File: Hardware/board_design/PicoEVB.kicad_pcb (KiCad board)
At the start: 4 copper layers, 22.5 x 30 mm, 107 parts, among them J1 RX-, J10 1P2, J11 1P0, J12 GND, J2 RX+, J3 CLKIN-, J4 CLKIN+, J5 TX+, J6 TX-, J7 3P3, J8 1P8, J9 1P0, P1 CONN_01X06, U1 XC7AxxT-xCSG325, U2 S25Q, U3 TPS82085SIL, U4 MAX1589AETT100T, U5 MIC47050-1.2YML, U6 TPS82085SIL, U7 FT230XQ

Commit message: configure project libararies
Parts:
- added REF**: VFBGA54, AS4C32M16MSA-6BIN:AS4C32M16MSA-6BIN, F.Cu at (84.9, 80.9)

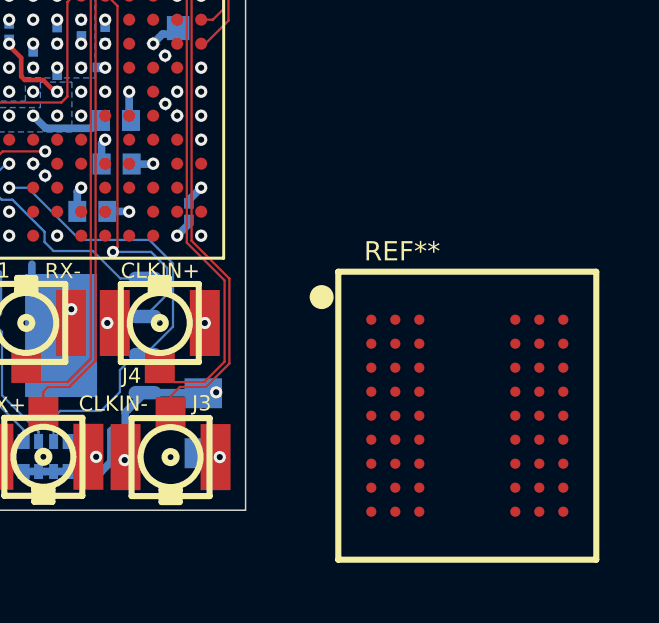
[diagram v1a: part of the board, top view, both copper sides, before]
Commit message: Added LPSDRAM
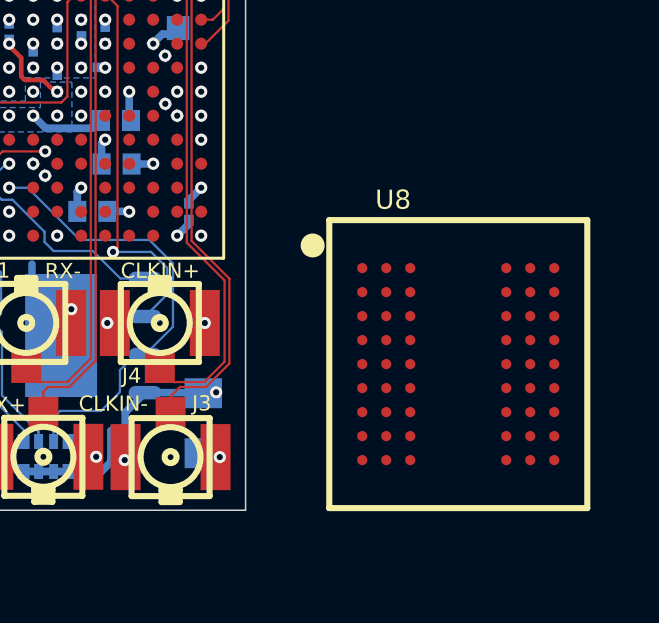
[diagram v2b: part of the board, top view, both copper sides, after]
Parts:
- removed REF**: VFBGA54, AS4C32M16MSA-6BIN:AS4C32M16MSA-6BIN
- added U8: VFBGA54, AS4C32M16MSA-6BIN:AS4C32M16MSA-6BIN, F.Cu at (84.6, 79.2)
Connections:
- PCB1 pad 55: (no net) -> Net-(PCB1-Pad55)
- RN1 pad 5: (no net) -> Net-(RN1-Pad5)
- RN3 pad 8: (no net) -> Net-(RN3-Pad8)
- U1 pad A15: (no net) -> Net-(U1-PadA15)
- U1 pad A17: (no net) -> Net-(U1-PadA17)
- U1 pad B10: (no net) -> Net-(U1-PadB10)
- U1 pad B11: (no net) -> Net-(U1-PadB11)
- U1 pad B14: (no net) -> Net-(U1-PadB14)
- U1 pad B15: (no net) -> Net-(U1-PadB15)
- U1 pad B16: (no net) -> Net-(U1-PadB16)
- U1 pad B17: (no net) -> Net-(U1-PadB17)
- U1 pad B9: (no net) -> Net-(U1-PadB9)
- U1 pad C11: (no net) -> Net-(U1-PadC11)
- U1 pad C12: (no net) -> Net-(U1-PadC12)
- U1 pad C13: (no net) -> Net-(U1-PadC13)
- U1 pad C14: (no net) -> Net-(U1-PadC14)
- U1 pad C16: (no net) -> Net-(U1-PadC16)
- U1 pad C17: (no net) -> Net-(U1-PadC17)
- U1 pad C18: (no net) -> Net-(U1-PadC18)
- U1 pad C8: (no net) -> Net-(U1-PadC8)
- U1 pad C9: (no net) -> Net-(U1-PadC9)
- U1 pad D10: (no net) -> Net-(U1-PadD10)
- U1 pad D11: (no net) -> Net-(U1-PadD11)
- U1 pad D13: (no net) -> Net-(U1-PadD13)
- U1 pad D14: (no net) -> Net-(U1-PadD14)
- U1 pad D15: (no net) -> Net-(U1-PadD15)
- U1 pad D16: (no net) -> Net-(U1-PadD16)
- U1 pad D18: (no net) -> Net-(U1-PadD18)
- U1 pad D8: (no net) -> Net-(U1-PadD8)
- U1 pad D9: (no net) -> Net-(U1-PadD9)
- U1 pad E13: (no net) -> Net-(U1-PadE13)
- U1 pad E15: (no net) -> Net-(U1-PadE15)
- U1 pad E16: (no net) -> Net-(U1-PadE16)
- U1 pad E17: (no net) -> Net-(U1-PadE17)
- U1 pad E18: (no net) -> Net-(U1-PadE18)
- U1 pad F1: (no net) -> Net-(U1-PadF1)
- U1 pad F14: (no net) -> Net-(U1-PadF14)
- U1 pad F15: (no net) -> Net-(U1-PadF15)
- U1 pad F17: (no net) -> Net-(U1-PadF17)
- U1 pad F18: (no net) -> Net-(U1-PadF18)
- U1 pad F2: (no net) -> Net-(U1-PadF2)
- U1 pad G14: (no net) -> Net-(U1-PadG14)
- U1 pad G15: (no net) -> Net-(U1-PadG15)
- U1 pad G16: (no net) -> Net-(U1-PadG16)
- U1 pad G17: (no net) -> Net-(U1-PadG17)
- U1 pad H14: (no net) -> Net-(U1-PadH14)
- U1 pad H16: (no net) -> Net-(U1-PadH16)
- U1 pad H17: (no net) -> Net-(U1-PadH17)
- U1 pad H18: (no net) -> Net-(U1-PadH18)
- U1 pad J14: (no net) -> Net-(U1-PadJ14)
- U1 pad J4: (no net) -> Net-(U1-PadJ4)
- U1 pad J5: (no net) -> Net-(U1-PadJ5)
- U1 pad J6: (no net) -> Net-(U1-PadJ6)
- U1 pad K15: (no net) -> Net-(U1-PadK15)
- U1 pad K17: (no net) -> Net-(U1-PadK17)
- U1 pad K18: (no net) -> Net-(U1-PadK18)
- U1 pad K3: (no net) -> Net-(U1-PadK3)
- U1 pad K5: (no net) -> Net-(U1-PadK5)
- U1 pad K6: (no net) -> Net-(U1-PadK6)
- U1 pad L14: (no net) -> Net-(U1-PadL14)
- U1 pad L18: (no net) -> Net-(U1-PadL18)
- U1 pad L2: (no net) -> Net-(U1-PadL2)
- U1 pad L3: (no net) -> Net-(U1-PadL3)
- U1 pad L4: (no net) -> Net-(U1-PadL4)
- U1 pad L5: (no net) -> Net-(U1-PadL5)
- U1 pad M1: (no net) -> Net-(U1-PadM1)
- U1 pad M14: (no net) -> Net-(U1-PadM14)
- U1 pad M15: (no net) -> Net-(U1-PadM15)
- U1 pad M16: (no net) -> Net-(U1-PadM16)
- U1 pad M17: (no net) -> Net-(U1-PadM17)
- U1 pad M2: (no net) -> Net-(U1-PadM2)
- U1 pad M4: (no net) -> Net-(U1-PadM4)
- U1 pad M5: (no net) -> Net-(U1-PadM5)
- U1 pad M6: (no net) -> Net-(U1-PadM6)
- U1 pad N1: (no net) -> Net-(U1-PadN1)
- U1 pad N14: (no net) -> Net-(U1-PadN14)
- U1 pad N16: (no net) -> Net-(U1-PadN16)
- U1 pad N17: (no net) -> Net-(U1-PadN17)
- U1 pad N18: (no net) -> Net-(U1-PadN18)
- U1 pad N2: (no net) -> Net-(U1-PadN2)
- U1 pad N3: (no net) -> Net-(U1-PadN3)
- U1 pad N4: (no net) -> Net-(U1-PadN4)
- U1 pad N6: (no net) -> Net-(U1-PadN6)
- U1 pad P1: (no net) -> Net-(U1-PadP1)
- U1 pad P14: (no net) -> Net-(U1-PadP14)
- U1 pad P15: (no net) -> Net-(U1-PadP15)
- U1 pad P16: (no net) -> Net-(U1-PadP16)
- U1 pad P18: (no net) -> Net-(U1-PadP18)
- U1 pad P3: (no net) -> Net-(U1-PadP3)
- U1 pad P4: (no net) -> Net-(U1-PadP4)
- U1 pad P5: (no net) -> Net-(U1-PadP5)
- U1 pad P6: (no net) -> Net-(U1-PadP6)
- U1 pad R1: (no net) -> Net-(U1-PadR1)
- U1 pad R13: (no net) -> Net-(U1-PadR13)
- U1 pad R15: (no net) -> Net-(U1-PadR15)
- U1 pad R16: (no net) -> Net-(U1-PadR16)
- U1 pad R17: (no net) -> Net-(U1-PadR17)
- U1 pad R18: (no net) -> Net-(U1-PadR18)
- U1 pad R2: (no net) -> Net-(U1-PadR2)
- U1 pad R3: (no net) -> Net-(U1-PadR3)
- U1 pad R5: (no net) -> Net-(U1-PadR5)
- U1 pad R6: (no net) -> Net-(U1-PadR6)
- U1 pad R7: (no net) -> Net-(U1-PadR7)
- U1 pad T12: (no net) -> Net-(U1-PadT12)
- U1 pad T13: (no net) -> Net-(U1-PadT13)
- U1 pad T14: (no net) -> Net-(U1-PadT14)
- U1 pad T15: (no net) -> Net-(U1-PadT15)
- U1 pad T17: (no net) -> Net-(U1-PadT17)
- U1 pad T18: (no net) -> Net-(U1-PadT18)
- U1 pad T2: (no net) -> Net-(U1-PadT2)
- U1 pad T3: (no net) -> Net-(U1-PadT3)
- U1 pad T4: (no net) -> Net-(U1-PadT4)
- U1 pad T5: (no net) -> Net-(U1-PadT5)
- U1 pad T7: (no net) -> Net-(U1-PadT7)
- U1 pad U1: (no net) -> Net-(U1-PadU1)
- U1 pad U10: (no net) -> Net-(U1-PadU10)
- U1 pad U11: (no net) -> Net-(U1-PadU11)
- U1 pad U12: (no net) -> Net-(U1-PadU12)
- U1 pad U14: (no net) -> Net-(U1-PadU14)
- U1 pad U15: (no net) -> Net-(U1-PadU15)
- U1 pad U16: (no net) -> Net-(U1-PadU16)
- U1 pad U17: (no net) -> Net-(U1-PadU17)
- U1 pad U2: (no net) -> Net-(U1-PadU2)
- U1 pad U4: (no net) -> Net-(U1-PadU4)
- U1 pad U5: (no net) -> Net-(U1-PadU5)
- U1 pad U6: (no net) -> Net-(U1-PadU6)
- U1 pad U7: (no net) -> Net-(U1-PadU7)
- U1 pad U9: (no net) -> Net-(U1-PadU9)
- U1 pad V11: (no net) -> Net-(U1-PadV11)
- U1 pad V16: (no net) -> Net-(U1-PadV16)
- U1 pad V17: (no net) -> Net-(U1-PadV17)
- U1 pad V4: (no net) -> Net-(U1-PadV4)
- U1 pad V6: (no net) -> Net-(U1-PadV6)
- U1 pad V7: (no net) -> Net-(U1-PadV7)
- U1 pad V8: (no net) -> Net-(U1-PadV8)
- U1 pad V9: (no net) -> Net-(U1-PadV9)
- U4 pad 2: (no net) -> Net-(U4-Pad2)
- U4 pad 3: (no net) -> Net-(U4-Pad3)
- U5 pad 5: (no net) -> Net-(U5-Pad5)
- U7 pad 11: (no net) -> Net-(U7-Pad11)
- U7 pad 12: (no net) -> Net-(U7-Pad12)
- U7 pad 14: (no net) -> Net-(U7-Pad14)
- U7 pad 5: (no net) -> Net-(U7-Pad5)

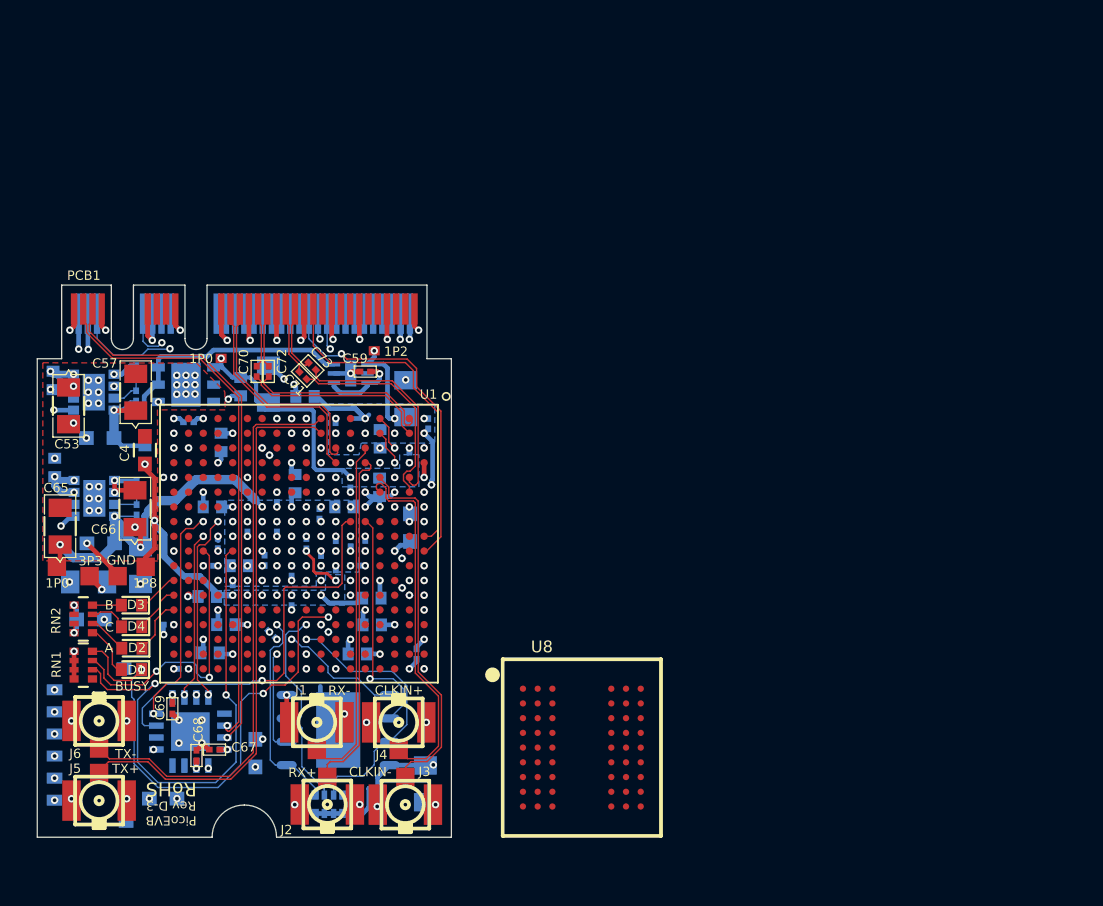
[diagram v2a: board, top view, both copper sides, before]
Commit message: populate LPSDRAM IC
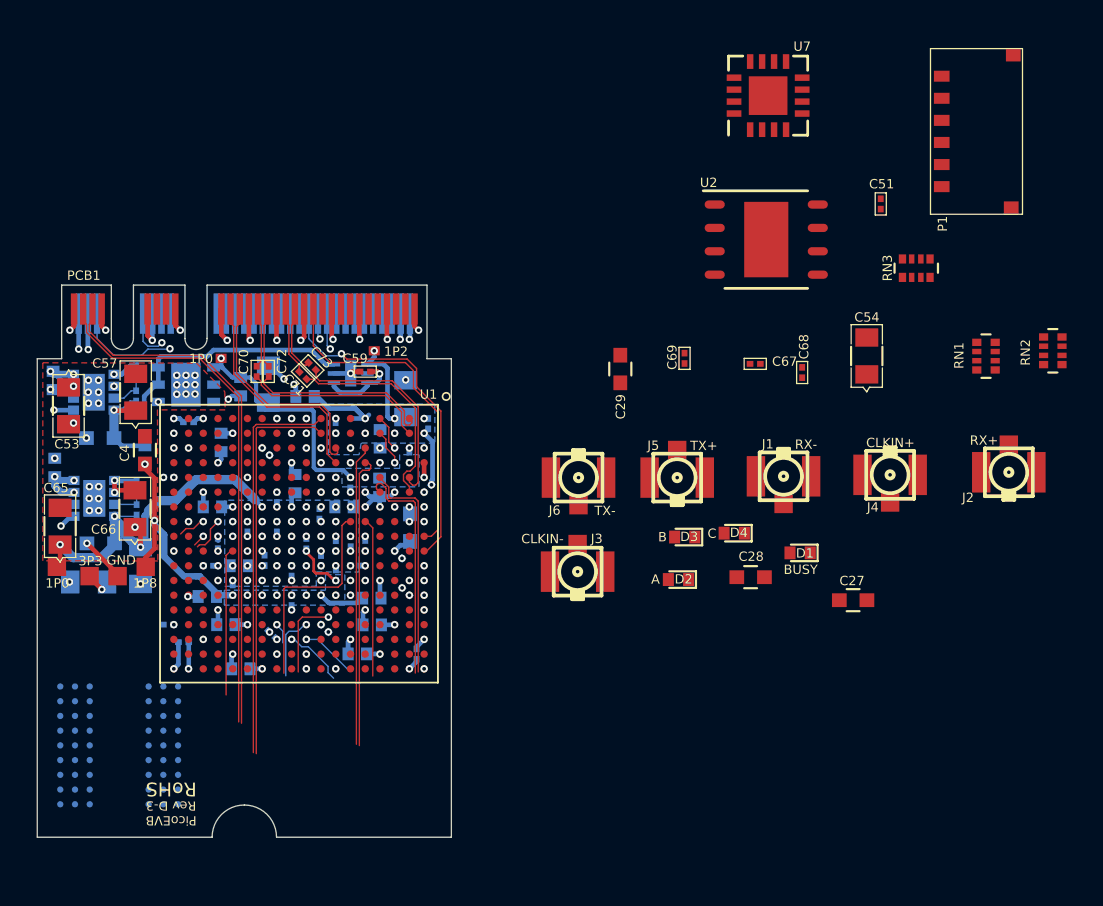
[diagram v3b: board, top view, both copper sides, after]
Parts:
- C27, C28, C29, C51, C54, P1, RN3, U2, U7: moved to F.Cu
- U8: moved to B.Cu
- moved P1 58.6 mm to (106.1, 45.7), turned to 90 degrees
- moved RN2 54.7 mm to (110.2, 57.6)
- moved RN1 51.8 mm to (106.6, 57.9)
- moved U7 46.7 mm to (94.7, 43.8), turned to 90 degrees
- moved RN3 43.2 mm to (102.8, 53.1), turned to 270 degrees
- moved C51 42.1 mm to (100.8, 49.7), turned to 90 degrees
- moved C27 41.5 mm to (99.3, 71.2)
- moved J2 41.2 mm to (107.8, 64.2)
- moved C68 38.9 mm to (96.6, 58.8)
- moved D1 36.9 mm to (96.5, 68.6)
- moved C67 36.1 mm to (94.0, 58.4)
- moved J5 36.0 mm to (89.8, 64.5)
- moved U2 35.4 mm to (94.6, 51.6)
- moved C28 34.1 mm to (93.8, 69.9)
- moved C69 33.7 mm to (90.2, 58.0)
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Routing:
- net Net-(D1-Pad1): track 31.0 -> 7.44 mm, vias 4 -> 2
- net Net-(RN1-Pad6): track 27.2 -> 8.04 mm, vias 2 -> 0
- net Net-(RN1-Pad7): track 15.3 -> 0.08 mm, vias 2 -> 0
- net VCC_BANK14_B: track 41.1 -> 27.9 mm, vias 50 -> 39
- net Net-(RN3-Pad7): track 15.1 -> 3.08 mm
- net GND: track 62.6 -> 51.0 mm, vias 165 -> 142
- net JTAG_TDO_B: track 12.3 -> 1.51 mm, vias 2 -> 1
- net Net-(RN3-Pad5): track 11.4 -> 1.12 mm
- net JTAG_TCK_B: track 21.5 -> 11.6 mm, vias 1 -> 0
- net /FPGA PCIe/UMGT0_TX+: track 31.1 -> 21.3 mm
- net /FPGA PCIe/UMGT0_TX-: track 31.1 -> 21.5 mm
- net Net-(RN3-Pad6): track 12.2 -> 3.58 mm
- net JTAG_TDI_B: track 9.20 -> 0.66 mm, vias 2 -> 1
- net JTAG_TMS_B: track 10.5 -> 2.02 mm, vias 2 -> 1
- net /FPGA PCIe/UMGTCLK_0-: track 19.8 -> 12.2 mm
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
